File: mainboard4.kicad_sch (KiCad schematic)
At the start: 11 parts, among them J12 USB3_A, J13 USB_C_Receptacle_USB2.0_16P, J8 Barrel_Jack

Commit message: add usb
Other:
- sheet USB2SATA ports: added VBUS; removed none
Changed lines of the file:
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@@
+	(wire
+		(pts
+			(xy 90.17 25.4) (xy 96.52 25.4)
+		)
+		(stroke
+			(width 0)
+			(type default)
+		)
+	)
 	(wire
 		(pts
@@
 	)
 	(label "VBUS"
-		(at 88.9 156.21 180)
+		(at 90.17 25.4 0)
+		(fields_autoplaced yes)
 		(effects
 			(font
 				(size 1.27 1.27)
 			)
-			(justify right bottom)
-		)
-	)
-	(label "nEXTRST"
-		(at 158.75 160.02 180)
+			(justify left bottom)
+		)
+	)
+	(label "VBUS"
+		(at 88.9 156.21 180)
+		(fields_autoplaced yes)
 		(effects
 			(font
@@
 		)
 	)
-	(label "VBUS"
-		(at 76.2 74.93 180)
+	(label "nEXTRST"
+		(at 158.75 160.02 180)
+		(fields_autoplaced yes)
 		(effects
 			(font
@@
 	)
 	(label "VBUS"
-		(at 77.47 40.64 180)
+		(at 76.2 74.93 180)
+		(fields_autoplaced yes)
 		(effects
 			(font
@@
 		)
 	)
-	(label "nEXTRST"
-		(at 152.4 153.67 0)
+	(label "VBUS"
+		(at 77.47 40.64 180)
+		(fields_autoplaced yes)
 		(effects
 			(font
 				(size 1.27 1.27)
 			)
+			(justify right bottom)
+		)
+	)
+	(label "nEXTRST"
+		(at 152.4 153.67 0)
+		(fields_autoplaced yes)
+		(effects
+			(font
+				(size 1.27 1.27)
+			)
 			(justify left bottom)
 		)
@@
 	(label "VBUS"
 		(at 153.67 148.59 0)
+		(fields_autoplaced yes)
 		(effects
 			(font
@@
 		(dnp no)
 		(fields_autoplaced yes)
-		(property "Reference" "#PWR80"
+		(property "Reference" "#PWR080"
 			(at 72.39 110.49 0)
 			(effects
@@
 			(project "mainboard4"
 				(path "/dd07ab80-a59c-44f4-ac7d-849e21e1384e"
-					(reference "#PWR80")
+					(reference "#PWR080")
 					(unit 1)
 				)
@@
 			(effects
 				(font
+					(size 1.27 1.27)
+				)
+				(justify left)
+			)
+		)
+		(pin "VBUS" input
+			(at 96.52 25.4 180)
+			(effects
+				(font

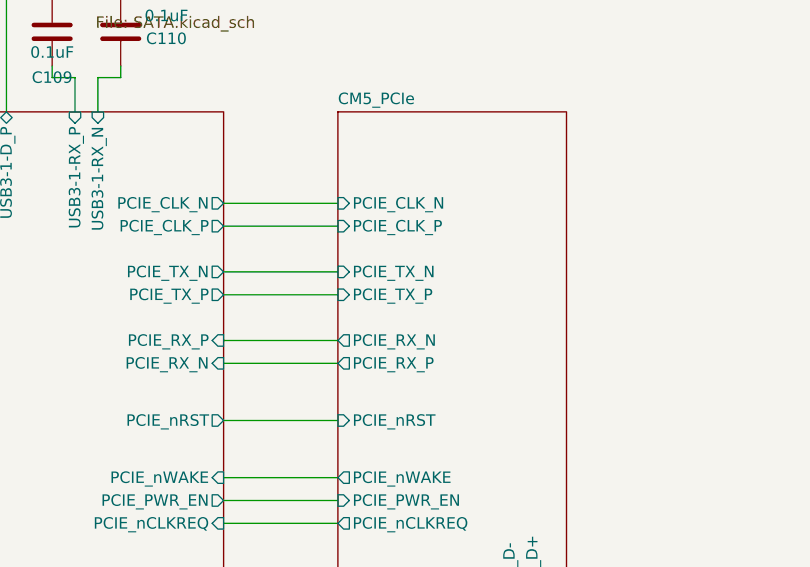
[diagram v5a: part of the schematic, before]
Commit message: add pcie line
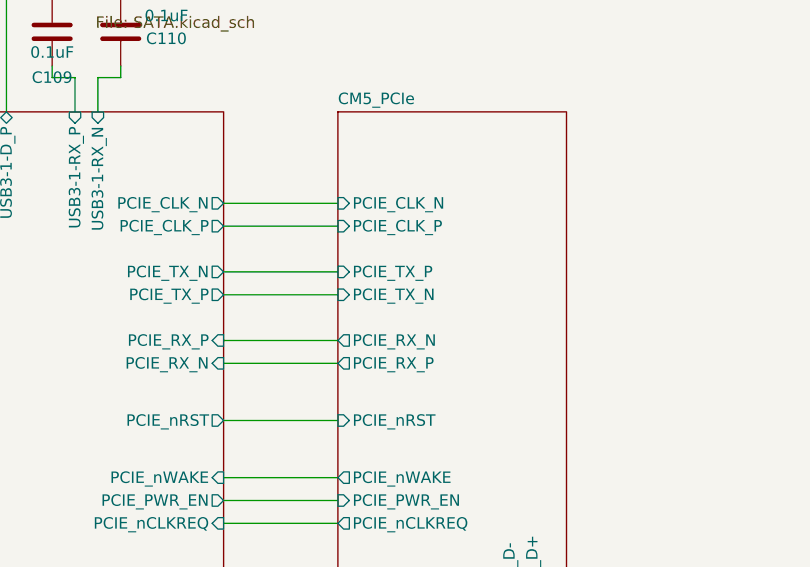
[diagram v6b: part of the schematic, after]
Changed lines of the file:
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@@
 			)
 		)
-		(pin "PCIE_TX_P" input
+		(pin "PCIE_TX_N" input
 			(at 162.56 76.2 180)
 			(effects
@@
 			)
 		)
-		(pin "PCIE_TX_N" input
+		(pin "PCIE_TX_P" input
 			(at 162.56 73.66 180)
 			(effects

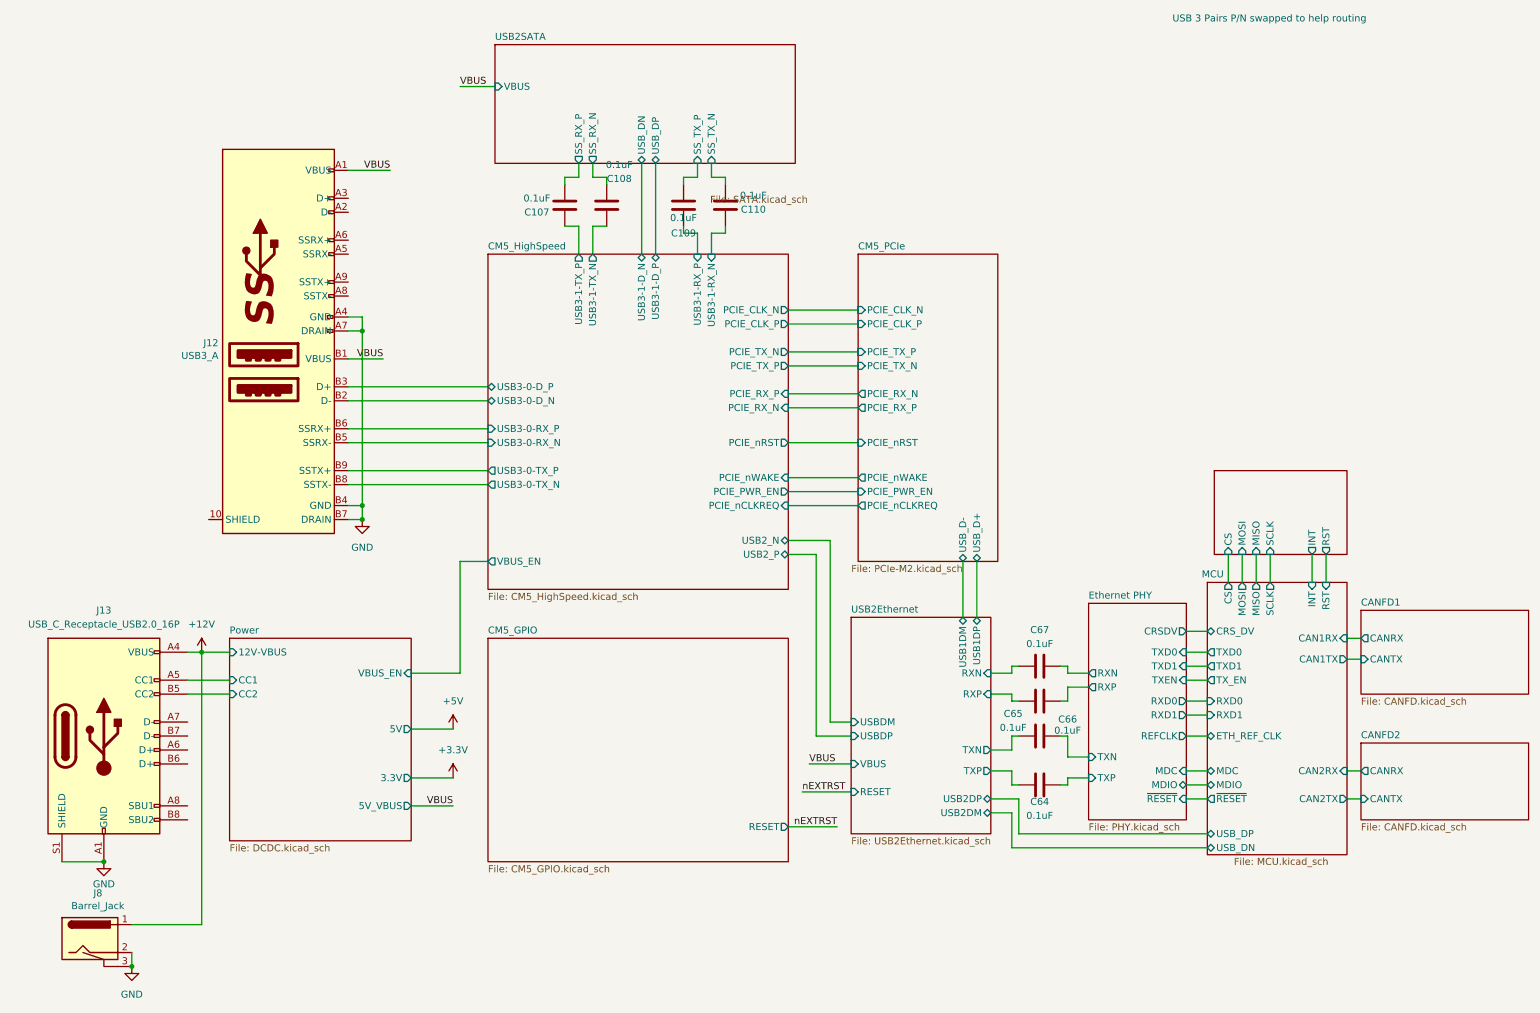
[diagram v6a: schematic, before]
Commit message: add usb2.0 line
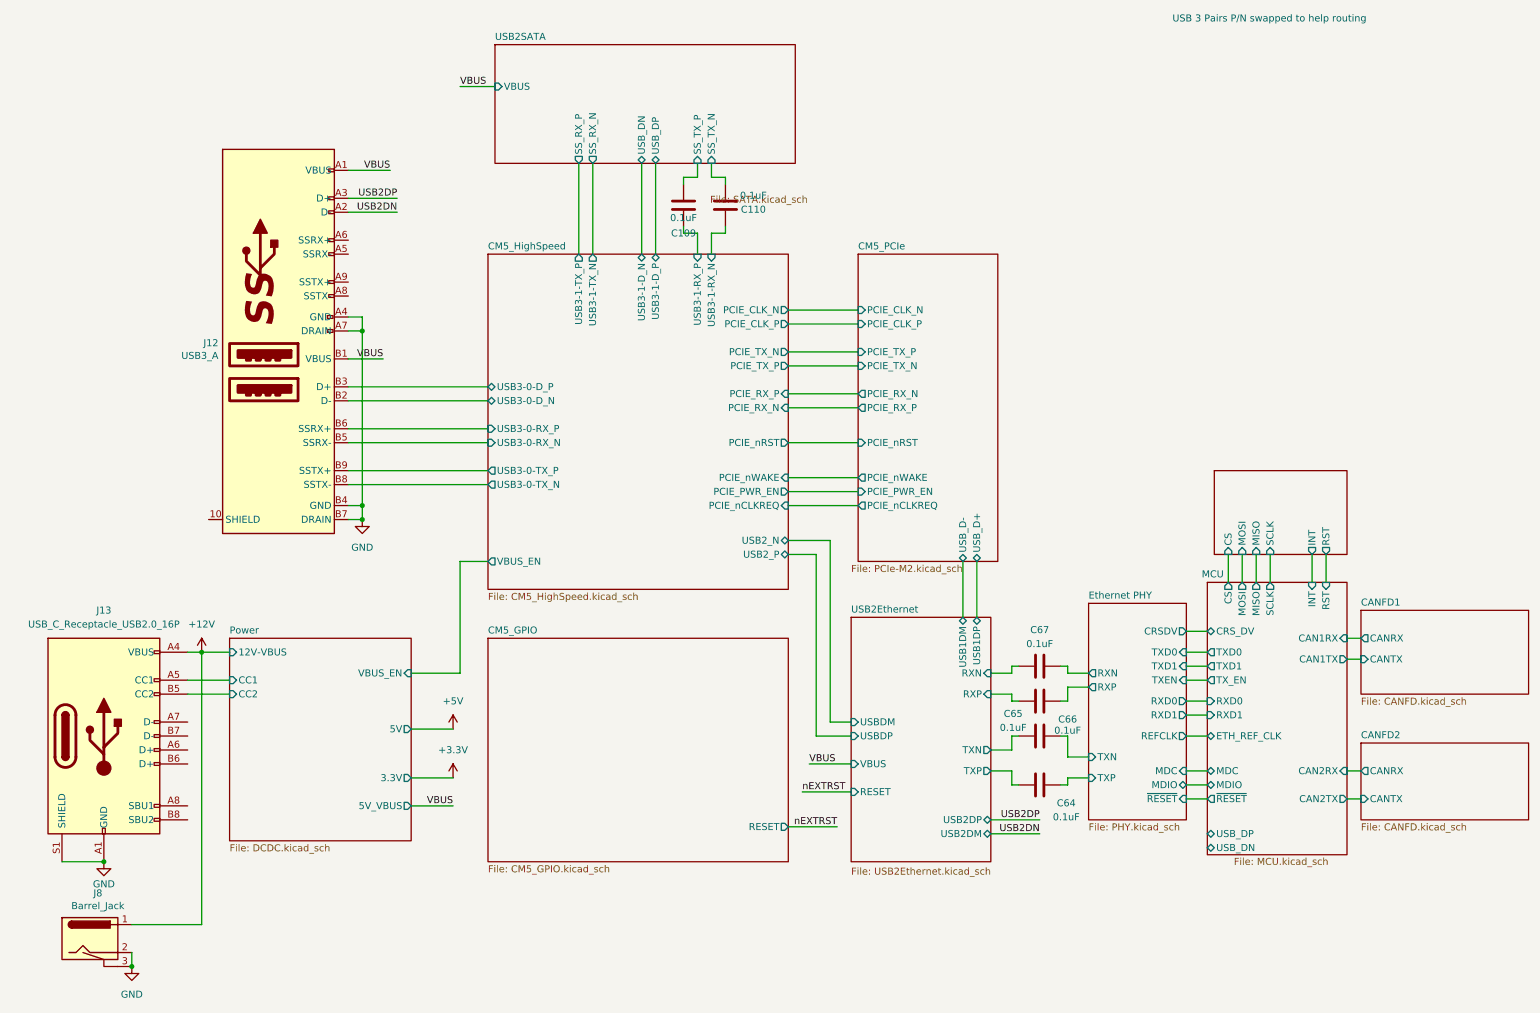
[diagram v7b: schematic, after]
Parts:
- removed C107, C108: 0.1uF, Capacitor_SMD:C_0402_1005Metric_Pad0.74x0.62mm_HandSolder, symbol Device:C
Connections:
- net USB2DN: now reaches J12.A2 (D-)
- net USB2DP: now reaches J12.A3 (D+)

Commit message: add HDD_LED[
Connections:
- net GND: now also J12.10 (SHIELD)
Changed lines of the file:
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@@
 	(label "VBUS"
 		(at 90.17 25.4 0)
-		(fields_autoplaced yes)
 		(effects
 			(font
@@
 	(label "VBUS"
 		(at 88.9 156.21 180)
-		(fields_autoplaced yes)
 		(effects
 			(font
@@
 	(label "nEXTRST"
 		(at 158.75 160.02 180)
-		(fields_autoplaced yes)
 		(effects
 			(font
@@
 	(label "USB2DP"
 		(at 195.58 158.75 180)
-		(fields_autoplaced yes)
 		(effects
 			(font
@@
 	(label "USB2DN"
 		(at 78.74 48.26 180)
-		(fields_autoplaced yes)
 		(effects
 			(font
@@
 	(label "USB2DP"
 		(at 78.74 45.72 180)
-		(fields_autoplaced yes)
 		(effects
 			(font
@@
 	(label "VBUS"
 		(at 76.2 74.93 180)
-		(fields_autoplaced yes)
 		(effects
 			(font
@@
 	(label "USB2DN"
 		(at 195.58 161.29 180)
-		(fields_autoplaced yes)
 		(effects
 			(font
@@
 	(label "VBUS"
 		(at 77.47 40.64 180)
-		(fields_autoplaced yes)
 		(effects
 			(font
@@
 	(label "nEXTRST"
 		(at 152.4 153.67 0)
-		(fields_autoplaced yes)
 		(effects
 			(font
@@
 	(label "VBUS"
 		(at 153.67 148.59 0)
-		(fields_autoplaced yes)
 		(effects
 			(font
@@
 					(unit 1)
 				)
+			)
+		)
+	)
+	(symbol
+		(lib_id "power:GND")
+		(at 44.45 104.14 0)
+		(unit 1)
+		(exclude_from_sim no)
+		(in_bom yes)
+		(on_board yes)
+		(dnp no)
+		(fields_autoplaced yes)
+		(property "Reference" "#PWR54"
+			(at 44.45 110.49 0)
+			(effects
+				(font
+					(size 1.27 1.27)
+				)
+				(hide yes)
+			)
+		)
+		(property "Value" "GND"
+			(at 44.45 109.22 0)
+			(effects
+				(font
+					(size 1.27 1.27)
+				)
+			)
+		)
+		(property "Footprint" ""
+			(at 44.45 104.14 0)
+			(effects
+				(font
+					(size 1.27 1.27)
+				)
+				(hide yes)
+			)
+		)
+		(property "Datasheet" ""
+			(at 44.45 104.14 0)
+			(effects
+				(font
+					(size 1.27 1.27)
+				)
+				(hide yes)
+			)
+		)
+		(property "Description" "Power symbol creates a global label with name \"GND\" , ground"
+			(at 44.45 104.14 0)
+			(effects
+				(font
+					(size 1.27 1.27)
+				)
+				(hide yes)
+			)
+		)
+		(pin "1"
+		)
+		(instances
+			(project "mainboard4"
+				(path "/dd07ab80-a59c-44f4-ac7d-849e21e1384e"
+					(reference "#PWR54")
+					(unit 1)
+				)
